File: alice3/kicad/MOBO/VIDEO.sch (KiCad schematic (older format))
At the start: 15 parts, among them SW1 RESET, U1 LM2937-3.3, U2 VGA_daughter_board, U3 Propeller_P8X32A-D40, U4 24LC256, U5 Propeller_Plug, Y1 5 MHz

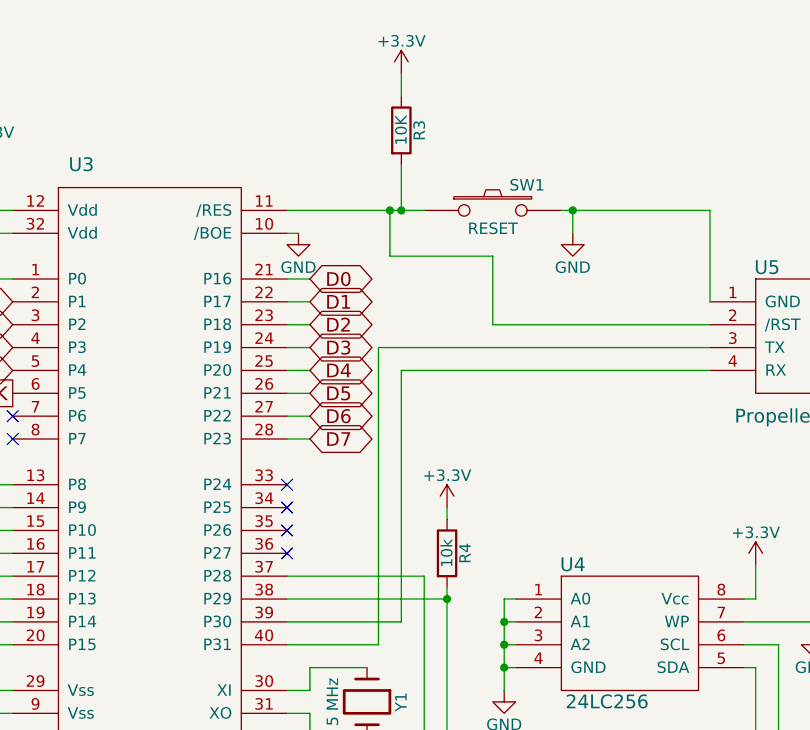
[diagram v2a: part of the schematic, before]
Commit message: Sync schematic with breadboard.
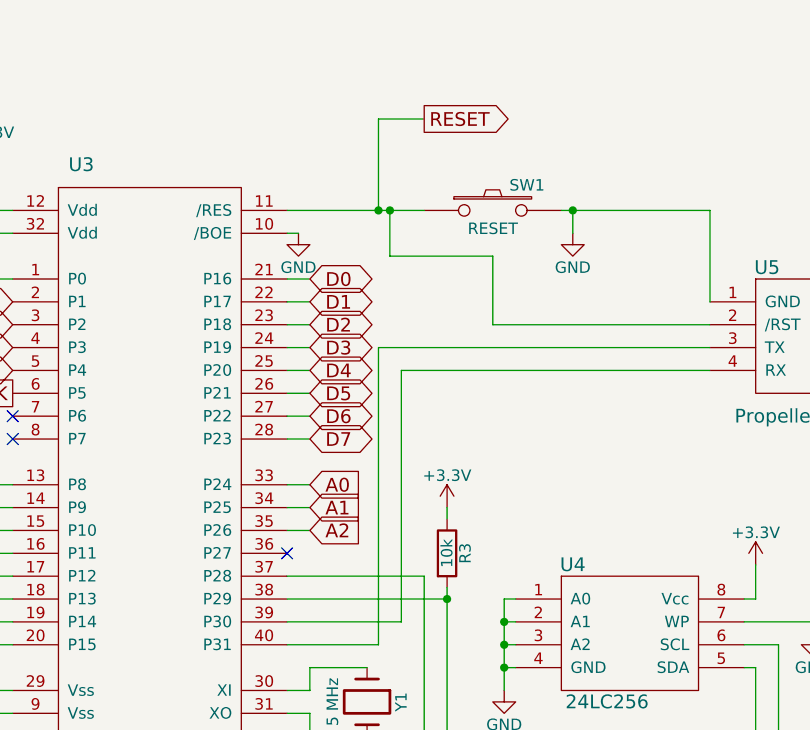
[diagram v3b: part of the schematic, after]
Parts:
- removed R3: 10K, Resistors_ThroughHole:Resistor_Horizontal_RM10mm, symbol R
- renumbered R4 to R3
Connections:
- net RESET: now reaches SW1.1, U3.11 (/RES), U5.2 (/RST)
- net A0: now reaches U3.33 (P24)
- net A1: now reaches U3.34 (P25)
- net A2: now reaches U3.35 (P26)
- no-connect marks 8 -> 5
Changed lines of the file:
@@
 EESchema Schematic File Version 2
+LIBS:sd_card
 LIBS:power
 LIBS:device
@@
 $EndComp
 $Comp
-L +3.3V #PWR03
-U 1 1 566E4B67
-P 7900 1700
-F 0 "#PWR03" H 7900 1550 50  0001 C CNN
-F 1 "+3.3V" H 7900 1840 50  0000 C CNN
-F 2 "" H 7900 1700 50  0000 C CNN
-F 3 "" H 7900 1700 50  0000 C CNN
-	1    7900 1700
-	1    0    0    -1
-$EndComp
-$Comp
-L R R3
-U 1 1 566E4B83
-P 7900 1950
-F 0 "R3" V 7980 1950 50  0000 C CNN
-F 1 "10K" V 7900 1950 50  0000 C CNN
-F 2 "Resistors_ThroughHole:Resistor_Horizontal_RM10mm" V 7830 1950 50  0001 C CNN
-F 3 "" H 7900 1950 50  0000 C CNN
-	1    7900 1950
-	1    0    0    -1
-$EndComp
-$Comp
 L SW_PUSH SW1
 U 1 1 566E4BAC
@@
 $EndComp
 $Comp
-L GND #PWR04
+L GND #PWR03
 U 1 1 566E4C07
 P 8650 2400
-F 0 "#PWR04" H 8650 2150 50  0001 C CNN
+F 0 "#PWR03" H 8650 2150 50  0001 C CNN
 F 1 "GND" H 8650 2250 50  0000 C CNN
 F 2 "" H 8650 2400 50  0000 C CNN
@@
 $EndComp
 $Comp
-L GND #PWR05
+L GND #PWR04
 U 1 1 5681F164
 P 8350 4400
-F 0 "#PWR05" H 8350 4150 50  0001 C CNN
+F 0 "#PWR04" H 8350 4150 50  0001 C CNN
 F 1 "GND" H 8350 4250 50  0000 C CNN
 F 2 "" H 8350 4400 50  0000 C CNN
@@
 $EndComp
 $Comp
-L +3.3V #PWR06
+L +3.3V #PWR05
 U 1 1 5681F2C2
 P 9450 3850
-F 0 "#PWR06" H 9450 3700 50  0001 C CNN
+F 0 "#PWR05" H 9450 3700 50  0001 C CNN
 F 1 "+3.3V" H 9450 3990 50  0000 C CNN
 F 2 "" H 9450 3850 50  0000 C CNN
@@
 $EndComp
 $Comp
-L GND #PWR07
+L GND #PWR06
 U 1 1 5681F2E8
 P 9700 4150
-F 0 "#PWR07" H 9700 3900 50  0001 C CNN
+F 0 "#PWR06" H 9700 3900 50  0001 C CNN
 F 1 "GND" H 9700 4000 50  0000 C CNN
 F 2 "" H 9700 4150 50  0000 C CNN
@@
 $EndComp
 $Comp
-L +3.3V #PWR08
+L +3.3V #PWR07
 U 1 1 5681F435
 P 8100 3600
-F 0 "#PWR08" H 8100 3450 50  0001 C CNN
+F 0 "#PWR07" H 8100 3450 50  0001 C CNN
 F 1 "+3.3V" H 8100 3740 50  0000 C CNN
 F 2 "" H 8100 3600 50  0000 C CNN
@@
 $EndComp
 $Comp
-L R R4
+L R R3
 U 1 1 5681F454
 P 8100 3800
-F 0 "R4" V 8180 3800 50  0000 C CNN
+F 0 "R3" V 8180 3800 50  0000 C CNN
 F 1 "10k" V 8100 3800 50  0000 C CNN
 F 2 "Resistors_ThroughHole:Resistor_Horizontal_RM10mm" V 8030 3800 50  0001 C CNN
@@
 $EndComp
 $Comp
-L GND #PWR09
+L GND #PWR08
 U 1 1 5681F91B
 P 2950 2350
-F 0 "#PWR09" H 2950 2100 50  0001 C CNN
+F 0 "#PWR08" H 2950 2100 50  0001 C CNN
 F 1 "GND" H 2950 2200 50  0000 C CNN
 F 2 "" H 2950 2350 50  0000 C CNN
@@
 $EndComp
 $Comp
-L +5V #PWR010
+L +5V #PWR09
 U 1 1 5681FA03
 P 2350 1650
-F 0 "#PWR010" H 2350 1500 50  0001 C CNN
+F 0 "#PWR09" H 2350 1500 50  0001 C CNN
 F 1 "+5V" H 2350 1790 50  0000 C CNN
 F 2 "" H 2350 1650 50  0000 C CNN
@@
 $EndComp
 $Comp
-L +3.3V #PWR011
+L +3.3V #PWR010
 U 1 1 5681FA32
 P 3550 1650
-F 0 "#PWR011" H 3550 1500 50  0001 C CNN
+F 0 "#PWR010" H 3550 1500 50  0001 C CNN
 F 1 "+3.3V" H 3550 1790 50  0000 C CNN
 F 2 "" H 3550 1650 50  0000 C CNN
@@
 $EndComp
 $Comp
-L GND #PWR012
+L GND #PWR011
 U 1 1 56821F3F
 P 5500 3100
-F 0 "#PWR012" H 5500 2850 50  0001 C CNN
+F 0 "#PWR011" H 5500 2850 50  0001 C CNN
 F 1 "GND" H 5500 2950 50  0000 C CNN
 F 2 "" H 5500 3100 50  0000 C CNN
@@
 NoConn ~ 7400 3800
 $Comp
-L GND #PWR013
+L GND #PWR012
 U 1 1 56826035
 P 7450 2400
-F 0 "#PWR013" H 7450 2150 50  0001 C CNN
+F 0 "#PWR012" H 7450 2150 50  0001 C CNN
 F 1 "GND" H 7450 2250 50  0000 C CNN
 F 2 "" H 7450 2400 50  0000 C CNN
@@
 	7400 2400 7450 2400
 Wire Wire Line
-	7900 1800 7900 1700
-Wire Wire Line
 	7400 2300 8000 2300
-Wire Wire Line
-	7900 2300 7900 2100
-Connection ~ 7900 2300
 Wire Wire Line
 	5500 3500 6200 3500
@@
 	9250 2800 8300 2800
 Wire Wire Line
-	7850 2500 7850 2300
-Connection ~ 7850 2300
+	7800 1900 7800 2300
+Connection ~ 7800 2300
 Wire Wire Line
 	9250 2900 7800 2900
@@
 	8300 2500 7850 2500
 $Comp
-L GND #PWR014
+L GND #PWR013
 U 1 1 568DCD28
 P 5600 4800
-F 0 "#PWR014" H 5600 4550 50  0001 C CNN
+F 0 "#PWR013" H 5600 4550 50  0001 C CNN
 F 1 "GND" H 5600 4650 50  0000 C CNN
 F 2 "" H 5600 4800 50  0000 C CNN
@@
 	5500 4800 5600 4800
 $Comp
-L +5V #PWR015
+L +5V #PWR014
 U 1 1 568DCDF3
 P 5900 4850
-F 0 "#PWR015" H 5900 4700 50  0001 C CNN
+F 0 "#PWR014" H 5900 4700 50  0001 C CNN
 F 1 "+5V" H 5900 4990 50  0000 C CNN
 F 2 "" H 5900 4850 50  0000 C CNN
@@
 Text GLabel 7500 3300 2    60   BiDi ~ 0
 D7
-NoConn ~ 7400 3500
-NoConn ~ 7400 3600
-NoConn ~ 7400 3700
 Text GLabel 6200 2700 0    60   Input ~ 0
 /IORQ
@@
 $EndComp
 $Comp
-L GND #PWR016
+L GND #PWR015
 U 1 1 568DD571
 P 5800 2200
-F 0 "#PWR016" H 5800 1950 50  0001 C CNN
+F 0 "#PWR015" H 5800 1950 50  0001 C CNN
 F 1 "GND" H 5800 2050 50  0000 C CNN
 F 2 "" H 5800 2200 50  0000 C CNN
@@
 $EndComp
 $Comp
-L +3.3V #PWR017
+L +3.3V #PWR016
 U 1 1 568DD5A9
 P 5800 1700
-F 0 "#PWR017" H 5800 1550 50  0001 C CNN
+F 0 "#PWR016" H 5800 1550 50  0001 C CNN
 F 1 "+3.3V" H 5800 1840 50  0000 C CNN
 F 2 "" H 5800 1700 50  0000 C CNN
@@
 Text GLabel 6200 3100 0    60   Output ~ 0
 CLK
+Text GLabel 7500 3500 2    60   Input ~ 0
+A0
+Text GLabel 7500 3600 2    60   Input ~ 0
+A1
+Text GLabel 7500 3700 2    60   Input ~ 0
+A2
+Wire Wire Line
+	7400 3500 7500 3500
+Wire Wire Line
+	7400 3600 7500 3600
+Wire Wire Line
+	7400 3700 7500 3700
+Text GLabel 8000 1900 2    60   Output ~ 0
+RESET
+Wire Wire Line
+	7800 1900 8000 1900
+Wire Wire Line
+	7850 2500 7850 2300
+Connection ~ 7850 2300
 $EndSCHEMATC

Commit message: Start PCB.
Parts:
- C1: footprint Capacitors_ThroughHole:C_Radial_D5_L6_P2.5 -> Capacitors_ThroughHole:C_Radial_D13_L21_P5
- C2: footprint (none) -> Capacitors_ThroughHole:C_Disc_D6_P5
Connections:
- net RESET renamed /RESET
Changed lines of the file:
@@
 F 0 "C1" H 3575 2100 50  0000 L CNN
 F 1 "1000 µF" H 3575 1900 50  0000 L CNN
-F 2 "Capacitors_ThroughHole:C_Radial_D5_L6_P2.5" H 3550 2000 50  0001 C CNN
+F 2 "Capacitors_ThroughHole:C_Radial_D13_L21_P5" H 3550 2000 50  0001 C CNN
 F 3 "" H 3550 2000 50  0000 C CNN
 	1    3550 2000
@@
 F 0 "C2" H 5825 2050 50  0000 L CNN
 F 1 "0.1 µF" H 5825 1850 50  0000 L CNN
-F 2 "" H 5838 1800 50  0000 C CNN
+F 2 "Capacitors_ThroughHole:C_Disc_D6_P5" H 5838 1800 50  0001 C CNN
 F 3 "" H 5800 1950 50  0000 C CNN
 	1    5800 1950
@@
 	7400 3700 7500 3700
 Text GLabel 8000 1900 2    60   Output ~ 0
-RESET
+/RESET
 Wire Wire Line
 	7800 1900 8000 1900

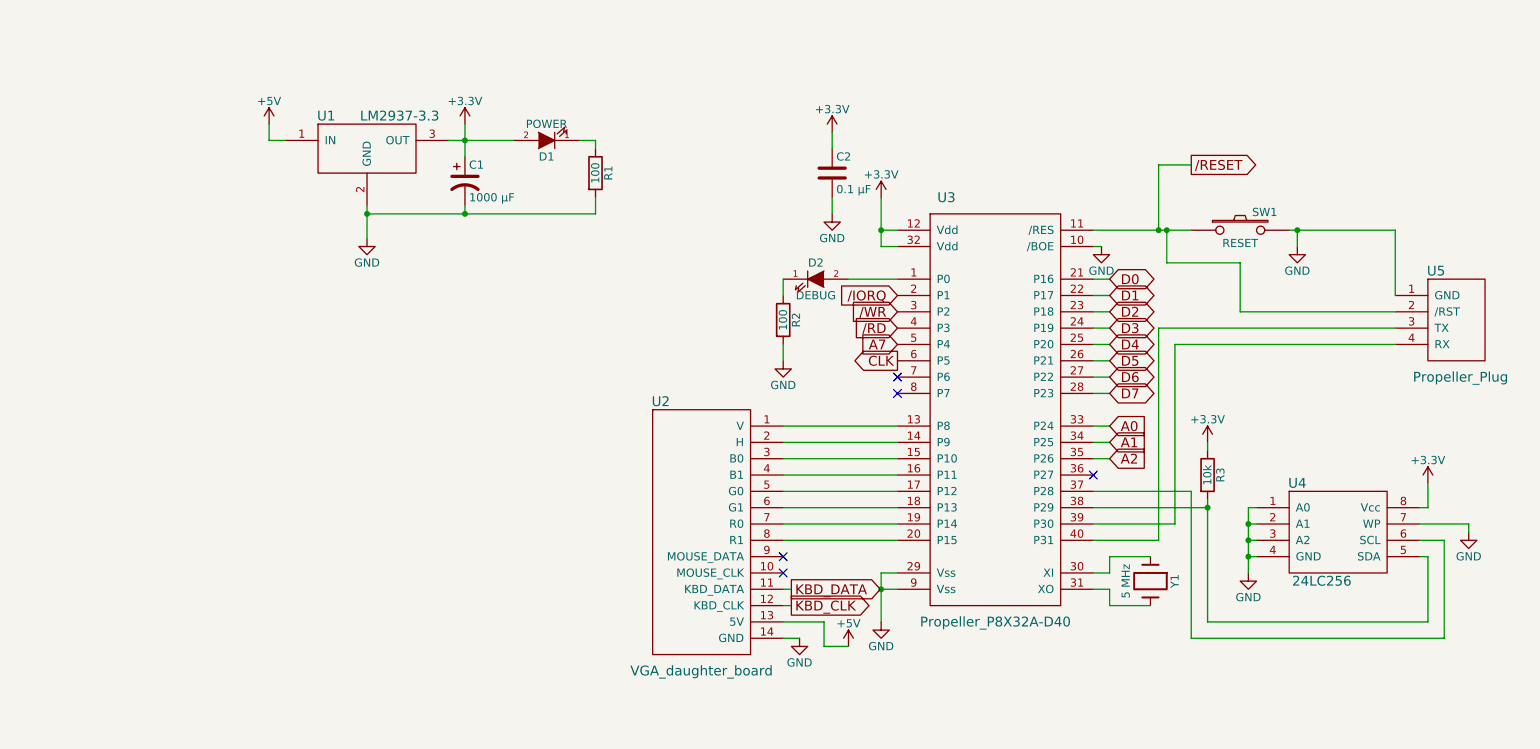
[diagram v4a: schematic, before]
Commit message: Add breakout header for 3 more prop pins.
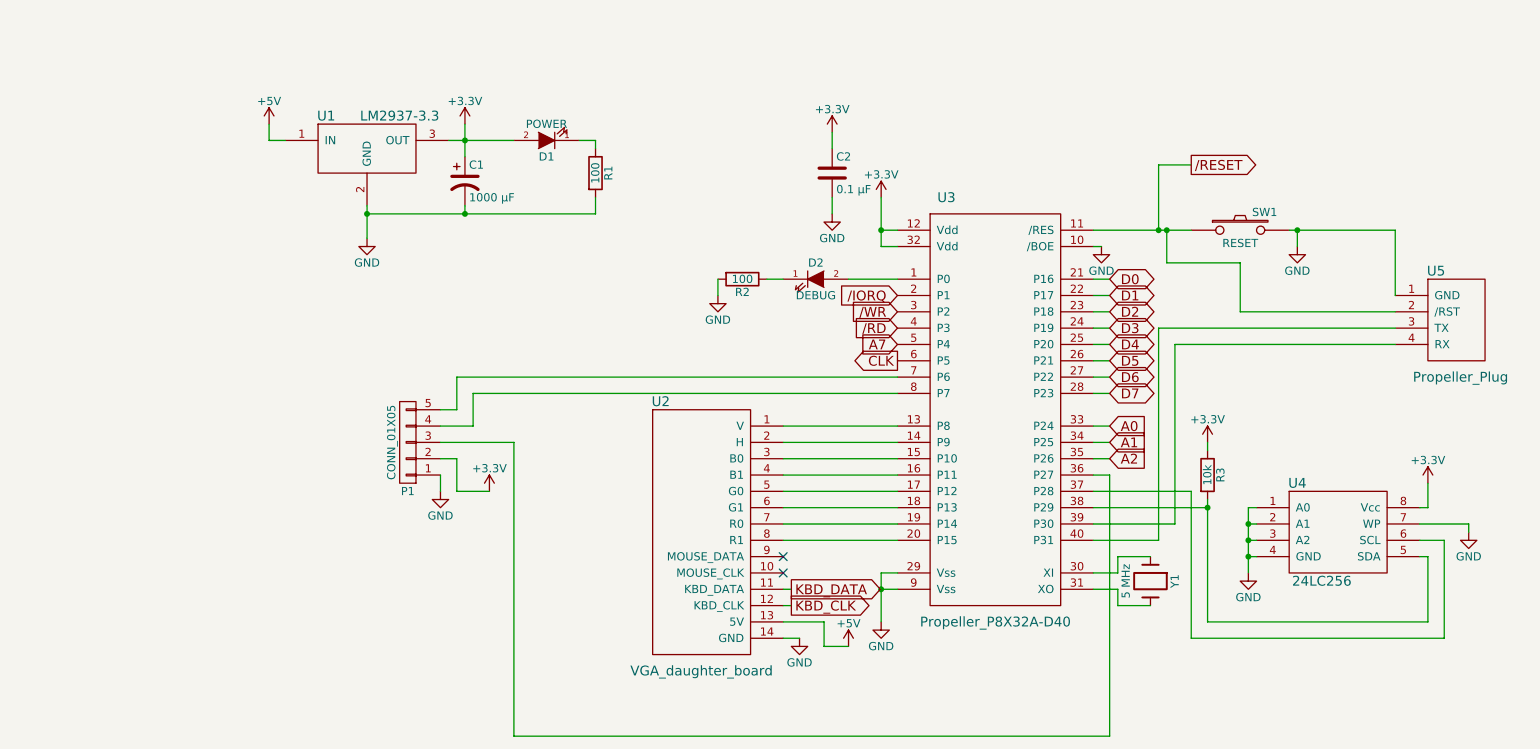
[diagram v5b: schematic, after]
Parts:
- added P1: CONN_01X05, symbol CONN_01X05
- U2: footprint Pin_Headers:Pin_Header_Straight_1x08 -> Pin_Headers:Pin_Header_Straight_1x14
- U3: footprint Housings_DIP:DIP-40_W25.4mm -> Housings_DIP:DIP-40_W15.24mm
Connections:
- net +3V3: now also P1.2 (P2)
- net GND: now also P1.1 (P1)
- net at U3.36 (P27): now also P1.3 (P3)
- net at U3.7 (P6): now also P1.5 (P5)
- net at U3.8 (P7): now also P1.4 (P4)
- no-connect marks 5 -> 2
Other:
- moved on the sheet: R2
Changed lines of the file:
@@
 F 0 "U3" H 6500 4700 60  0000 C CNN
 F 1 "Propeller_P8X32A-D40" H 6800 2100 60  0000 C CNN
-F 2 "Housings_DIP:DIP-40_W25.4mm" H 6800 3200 60  0001 C CNN
+F 2 "Housings_DIP:DIP-40_W15.24mm" H 6800 3200 60  0001 C CNN
 F 3 "" H 6800 3200 60  0000 C CNN
 	1    6800 3400
@@
 $EndComp
 $Comp
-L GND #PWR01
+L GND #PWR10
 U 1 1 566E4A0D
 P 6100 4700
-F 0 "#PWR01" H 6100 4450 50  0001 C CNN
+F 0 "#PWR10" H 6100 4450 50  0001 C CNN
 F 1 "GND" H 6100 4550 50  0000 C CNN
 F 2 "" H 6100 4700 50  0000 C CNN
@@
 $EndComp
 $Comp
-L +3.3V #PWR02
+L +3.3V #PWR9
 U 1 1 566E4A37
 P 6100 2100
-F 0 "#PWR02" H 6100 1950 50  0001 C CNN
+F 0 "#PWR9" H 6100 1950 50  0001 C CNN
 F 1 "+3.3V" H 6100 2240 50  0000 C CNN
 F 2 "" H 6100 2100 50  0000 C CNN
@@
 $EndComp
 $Comp
-L GND #PWR03
+L GND #PWR14
 U 1 1 566E4C07
 P 8650 2400
-F 0 "#PWR03" H 8650 2150 50  0001 C CNN
+F 0 "#PWR14" H 8650 2150 50  0001 C CNN
 F 1 "GND" H 8650 2250 50  0000 C CNN
 F 2 "" H 8650 2400 50  0000 C CNN
@@
 F 0 "U2" H 4750 4950 60  0000 C CNN
 F 1 "VGA_daughter_board" H 5000 3300 60  0000 C CNN
-F 2 "Pin_Headers:Pin_Header_Straight_1x08" H 5000 4200 60  0001 C CNN
+F 2 "Pin_Headers:Pin_Header_Straight_1x14" H 5000 4200 60  0001 C CNN
 F 3 "" H 5000 4200 60  0000 C CNN
 	1    5000 4150
@@
 $EndComp
 $Comp
-L GND #PWR04
+L GND #PWR13
 U 1 1 5681F164
 P 8350 4400
-F 0 "#PWR04" H 8350 4150 50  0001 C CNN
+F 0 "#PWR13" H 8350 4150 50  0001 C CNN
 F 1 "GND" H 8350 4250 50  0000 C CNN
 F 2 "" H 8350 4400 50  0000 C CNN
@@
 $EndComp
 $Comp
-L +3.3V #PWR05
+L +3.3V #PWR15
 U 1 1 5681F2C2
 P 9450 3850
-F 0 "#PWR05" H 9450 3700 50  0001 C CNN
+F 0 "#PWR15" H 9450 3700 50  0001 C CNN
 F 1 "+3.3V" H 9450 3990 50  0000 C CNN
 F 2 "" H 9450 3850 50  0000 C CNN
@@
 $EndComp
 $Comp
-L GND #PWR06
+L GND #PWR16
 U 1 1 5681F2E8
 P 9700 4150
-F 0 "#PWR06" H 9700 3900 50  0001 C CNN
+F 0 "#PWR16" H 9700 3900 50  0001 C CNN
 F 1 "GND" H 9700 4000 50  0000 C CNN
 F 2 "" H 9700 4150 50  0000 C CNN
@@
 $EndComp
 $Comp
-L +3.3V #PWR07
+L +3.3V #PWR12
 U 1 1 5681F435
 P 8100 3600
-F 0 "#PWR07" H 8100 3450 50  0001 C CNN
+F 0 "#PWR12" H 8100 3450 50  0001 C CNN
 F 1 "+3.3V" H 8100 3740 50  0000 C CNN
 F 2 "" H 8100 3600 50  0000 C CNN
@@
 $EndComp
 $Comp
-L GND #PWR08
+L GND #PWR2
 U 1 1 5681F91B
 P 2950 2350
-F 0 "#PWR08" H 2950 2100 50  0001 C CNN
+F 0 "#PWR2" H 2950 2100 50  0001 C CNN
 F 1 "GND" H 2950 2200 50  0000 C CNN
 F 2 "" H 2950 2350 50  0000 C CNN
@@
 $EndComp
 $Comp
-L +5V #PWR09
+L +5V #PWR1
 U 1 1 5681FA03
 P 2350 1650
-F 0 "#PWR09" H 2350 1500 50  0001 C CNN
+F 0 "#PWR1" H 2350 1500 50  0001 C CNN
 F 1 "+5V" H 2350 1790 50  0000 C CNN
 F 2 "" H 2350 1650 50  0000 C CNN
@@
 $EndComp
 $Comp
-L +3.3V #PWR010
+L +3.3V #PWR3
 U 1 1 5681FA32
 P 3550 1650
-F 0 "#PWR010" H 3550 1500 50  0001 C CNN
+F 0 "#PWR3" H 3550 1500 50  0001 C CNN
 F 1 "+3.3V" H 3550 1790 50  0000 C CNN
 F 2 "" H 3550 1650 50  0000 C CNN
@@
 L R R2
 U 1 1 56821F00
-P 5500 2850
-F 0 "R2" V 5580 2850 50  0000 C CNN
-F 1 "100" V 5500 2850 50  0000 C CNN
-F 2 "Resistors_ThroughHole:Resistor_Horizontal_RM10mm" V 5430 2850 50  0001 C CNN
-F 3 "" H 5500 2850 50  0000 C CNN
-	1    5500 2850
-	1    0    0    -1
-$EndComp
-$Comp
-L GND #PWR011
+P 5250 2600
+F 0 "R2" V 5330 2600 50  0000 C CNN
+F 1 "100" V 5250 2600 50  0000 C CNN
+F 2 "Resistors_ThroughHole:Resistor_Horizontal_RM10mm" V 5180 2600 50  0001 C CNN
+F 3 "" H 5250 2600 50  0000 C CNN
+	1    5250 2600
+	0    1    1    0
+$EndComp
+$Comp
+L GND #PWR4
 U 1 1 56821F3F
-P 5500 3100
-F 0 "#PWR011" H 5500 2850 50  0001 C CNN
-F 1 "GND" H 5500 2950 50  0000 C CNN
-F 2 "" H 5500 3100 50  0000 C CNN
-F 3 "" H 5500 3100 50  0000 C CNN
-	1    5500 3100
-	1    0    0    -1
-$EndComp
-NoConn ~ 6200 3300
-NoConn ~ 7400 3800
-$Comp
-L GND #PWR012
+P 5100 2700
+F 0 "#PWR4" H 5100 2450 50  0001 C CNN
+F 1 "GND" H 5100 2550 50  0000 C CNN
+F 2 "" H 5100 2700 50  0000 C CNN
+F 3 "" H 5100 2700 50  0000 C CNN
+	1    5100 2700
+	1    0    0    -1
+$EndComp
+$Comp
+L GND #PWR11
 U 1 1 56826035
 P 7450 2400
-F 0 "#PWR012" H 7450 2150 50  0001 C CNN
+F 0 "#PWR11" H 7450 2150 50  0001 C CNN
 F 1 "GND" H 7450 2250 50  0000 C CNN
 F 2 "" H 7450 2400 50  0000 C CNN
@@
 Connection ~ 6100 2300
 Wire Wire Line
-	7400 4400 7500 4400
-Wire Wire Line
-	7500 4400 7500 4300
-Wire Wire Line
-	7500 4300 7750 4300
-Wire Wire Line
-	7400 4500 7500 4500
-Wire Wire Line
-	7500 4500 7500 4600
-Wire Wire Line
-	7500 4600 7750 4600
+	7400 4400 7550 4400
+Wire Wire Line
+	7550 4400 7550 4300
+Wire Wire Line
+	7550 4300 7750 4300
+Wire Wire Line
+	7400 4500 7550 4500
+Wire Wire Line
+	7550 4500 7550 4600
+Wire Wire Line
+	7550 4600 7750 4600
 Wire Wire Line
 	7400 2400 7450 2400
@@
 Connection ~ 3550 2200
 Wire Wire Line
-	5500 2700 5500 2600
-Wire Wire Line
 	5900 2600 6200 2600
 Wire Wire Line
-	5500 3100 5500 3000
-Wire Wire Line
 	7400 2600 7500 2600
 Wire Wire Line
@@
 	8300 2500 7850 2500
 $Comp
-L GND #PWR013
+L GND #PWR5
 U 1 1 568DCD28
 P 5600 4800
-F 0 "#PWR013" H 5600 4550 50  0001 C CNN
+F 0 "#PWR5" H 5600 4550 50  0001 C CNN
 F 1 "GND" H 5600 4650 50  0000 C CNN
 F 2 "" H 5600 4800 50  0000 C CNN
@@
 	5500 4800 5600 4800
 $Comp
-L +5V #PWR014
+L +5V #PWR8
 U 1 1 568DCDF3
 P 5900 4850
-F 0 "#PWR014" H 5900 4700 50  0001 C CNN
+F 0 "#PWR8" H 5900 4700 50  0001 C CNN
 F 1 "+5V" H 5900 4990 50  0000 C CNN
 F 2 "" H 5900 4850 50  0000 C CNN
@@
 Text GLabel 6200 3000 0    60   Input ~ 0
 A7
-NoConn ~ 6200 3200
 Text GLabel 6200 2900 0    60   Input ~ 0
 /RD
@@
 $EndComp
 $Comp
-L GND #PWR015
+L GND #PWR7
 U 1 1 568DD571
 P 5800 2200
-F 0 "#PWR015" H 5800 1950 50  0001 C CNN
+F 0 "#PWR7" H 5800 1950 50  0001 C CNN
 F 1 "GND" H 5800 2050 50  0000 C CNN
 F 2 "" H 5800 2200 50  0000 C CNN
@@
 $EndComp
 $Comp
-L +3.3V #PWR016
+L +3.3V #PWR6
 U 1 1 568DD5A9
 P 5800 1700
-F 0 "#PWR016" H 5800 1550 50  0001 C CNN
+F 0 "#PWR6" H 5800 1550 50  0001 C CNN
 F 1 "+3.3V" H 5800 1840 50  0000 C CNN
 F 2 "" H 5800 1700 50  0000 C CNN
@@
 	7850 2500 7850 2300
 Connection ~ 7850 2300
+Wire Wire Line
+	5500 2600 5400 2600
+Wire Wire Line
+	5100 2600 5100 2700
+Wire Wire Line
+	6200 3200 3500 3200
+Wire Wire Line
+	3500 3200 3500 3400
+Wire Wire Line
+	3500 3400 3400 3400
+Wire Wire Line
+	6200 3300 3600 3300
+Wire Wire Line
+	3600 3300 3600 3500
+Wire Wire Line
+	3600 3500 3400 3500
+Wire Wire Line
+	7400 3800 7500 3800
+Wire Wire Line
+	7500 3800 7500 5400
+Wire Wire Line
+	7500 5400 3850 5400
+Wire Wire Line
+	3850 5400 3850 3600
+Wire Wire Line
+	3850 3600 3400 3600
+$Comp
+L CONN_01X05 P1
+U 1 1 56A04EF8
+P 3200 3600
+F 0 "P1" H 3200 3900 50  0000 C CNN
+F 1 "CONN_01X05" V 3300 3600 50  0000 C CNN
+F 2 "" H 3200 3600 50  0000 C CNN
+F 3 "" H 3200 3600 50  0000 C CNN
+	1    3200 3600
+	-1   0    0    1
+$EndComp
+$Comp
+L GND #PWR?
+U 1 1 56A0506B
+P 3400 3900
+F 0 "#PWR?" H 3400 3650 50  0001 C CNN
+F 1 "GND" H 3400 3750 50  0000 C CNN
+F 2 "" H 3400 3900 50  0000 C CNN
+F 3 "" H 3400 3900 50  0000 C CNN
+	1    3400 3900
+	1    0    0    -1
+$EndComp
+$Comp
+L +3.3V #PWR?
+U 1 1 56A050A3
+P 3700 3900
+F 0 "#PWR?" H 3700 3750 50  0001 C CNN
+F 1 "+3.3V" H 3700 4040 50  0000 C CNN
+F 2 "" H 3700 3900 50  0000 C CNN
+F 3 "" H 3700 3900 50  0000 C CNN
+	1    3700 3900
+	1    0    0    -1
+$EndComp
+Wire Wire Line
+	3400 3700 3500 3700
+Wire Wire Line
+	3500 3700 3500 3900
+Wire Wire Line
+	3500 3900 3700 3900
+Wire Wire Line
+	3400 3800 3400 3900
 $EndSCHEMATC
